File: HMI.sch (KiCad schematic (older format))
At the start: 0 parts

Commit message: Added Polyfuses and replace diodes
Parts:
- added C? (x4): 1nF, Capacitor_SMD:C_0603_1608Metric, symbol Device:C
- added F? (x2): SR010, Fuse:Fuse_0805_2012Metric, symbol Device:Polyfuse
- added F?: SR050, Fuse:Fuse_0805_2012Metric, symbol Device:Polyfuse
- added J?: Display, Connector_JST:JST_PH_B10B-PH-K_1x10_P2.00mm_Vertical, symbol Connector:Conn_01x10_Male
- added J?: SPI Interface, Connector_JST:JST_PH_B5B-PH-K_1x05_P2.00mm_Vertical, symbol Connector:Conn_01x05_Male
- added J?: I2C Interface, Connector_JST:JST_PH_B5B-PH-K_1x04_P2.00mm_Vertical, symbol Connector:Conn_01x04_Male
- added J?: Key 2, Connector_JST:JST_PH_B2B-PH-K_1x02_P2.00mm_Vertical, symbol Connector:Conn_01x02_Male
- added J?: Key 3, Connector_JST:JST_PH_B2B-PH-K_1x02_P2.00mm_Vertical, symbol Connector:Conn_01x02_Male
- added J?: Key 4, Connector_JST:JST_PH_B2B-PH-K_1x02_P2.00mm_Vertical, symbol Connector:Conn_01x02_Male
- added J?: Key 1, Connector_JST:JST_PH_B2B-PH-K_1x02_P2.00mm_Vertical, symbol Connector:Conn_01x02_Male
- added J?: LED3, Connector_JST:JST_PH_B2B-PH-K_1x02_P2.00mm_Vertical, symbol Connector:Conn_01x02_Male
- added J?: LED4, Connector_JST:JST_PH_B2B-PH-K_1x02_P2.00mm_Vertical, symbol Connector:Conn_01x02_Male
- added Q? (x2): BC817, Package_TO_SOT_SMD:SOT-23, symbol Transistor_BJT:BC817
- added R? (x2): 2.2kΩ, symbol Device:R
- added R? (x4): 4.7kΩ, Resistor_SMD:R_0603_1608Metric, symbol Device:R
- added R? (x4): 1kΩ, Resistor_SMD:R_0603_1608Metric, symbol Device:R
- added R? (x2): 4.7kΩ, symbol Device:R
- added R? (x2): 330Ω, symbol Device:R
- added RN? (x2): 330Ω, symbol Device:R_Pack04
- added U?: 74HC245, symbol 74xx:74HC245
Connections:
- new net: F?.2, J?.1 (Pin_1) (x3)
- new net: J?.2 (Pin_2), RN?.4 (R4.1)
- new net: J?.3 (Pin_3), RN?.3 (R3.1)
- new net: J?.4 (Pin_4), RN?.2 (R2.1)
- new net: J?.5 (Pin_5), RN?.1 (R1.1)
- new net: J?.6 (Pin_6), RN?.4 (R4.1)
- new net: J?.7 (Pin_7), RN?.3 (R3.1)
- new net: J?.8 (Pin_8), RN?.2 (R2.1)
- new net: RN?.8 (R1.2), U?.11 (B7)
- new net: RN?.7 (R2.2), U?.12 (B6)
- new net: RN?.6 (R3.2), U?.13 (B5)
- new net: RN?.5 (R4.2), U?.14 (B4)
- new net: RN?.8 (R1.2), U?.15 (B3)
- new net: RN?.7 (R2.2), U?.16 (B2)
- new net: RN?.6 (R3.2), U?.17 (B1)
- new net: RN?.5 (R4.2), U?.18 (B0)
- new net: J?.1 (Pin_1), R?.1, R?.2 (x4)
- new net: Q?.1 (B), R?.1 (x2)
- new net: J?.1 (Pin_1), R?.1 (x2)
- new net: J?.2 (Pin_2), Q?.3 (C) (x2)
- new net +3V3: F?.1, R?.1, R?.1
- new net +5V: F?.1, F?.1, R?.2, R?.2, R?.2, R?.2, R?.2, R?.2, U?.1 (A->B), U?.20 (VCC)
- new net GND: C?.2, C?.2, C?.2, C?.2, J?.10 (Pin_10), J?.2 (Pin_2), J?.2 (Pin_2), J?.2 (Pin_2), J?.2 (Pin_2), J?.3 (Pin_3), J?.5 (Pin_5), J?.9 (Pin_9), Q?.2 (E), Q?.2 (E), U?.10 (GND), U?.19 (CE)
- new net I2C_SCL: J?.4 (Pin_4), R?.2
- new net I2C_SDA: J?.2 (Pin_2), R?.2
- new net KEY_1: C?.1, R?.1
- new net KEY_2: C?.1, R?.1
- new net KEY_3: C?.1, R?.1
- new net KEY_4: C?.1, R?.1
- new net LCD_CON: U?.8 (A6)
- new net LCD_DB4: U?.4 (A2)
- new net LCD_DB5: U?.5 (A3)
- new net LCD_DB6: U?.6 (A4)
- new net LCD_DB7: U?.7 (A5)
- new net LCD_E: U?.3 (A1)
- new net LCD_RS: U?.2 (A0)
- new net LED3: R?.2
- new net LED4: R?.2
- new net MISO: J?.4 (Pin_4), U?.9 (A7)
- new net SPI_MISO: RN?.1 (R1.1)
- new net SPI_MOSI_BUF: J?.2 (Pin_2)
- new net SPI_SCLK_BUF: J?.3 (Pin_3)
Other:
- note added: "Buffered outputs signals"
- note added: "Check if switching is fast enought"
- note added: "Optional Keys input"
- note added: "RC Debounce"
- note added: "Wyświetlacz HD44780"
- note added: "Złącza JST PH"

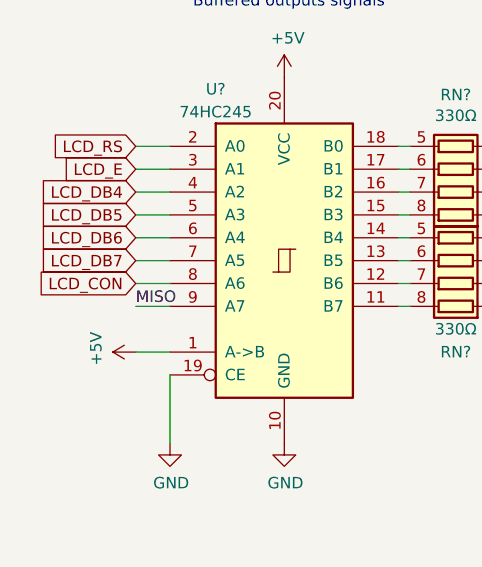
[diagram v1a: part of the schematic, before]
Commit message: Added USB B socket with ESD filter
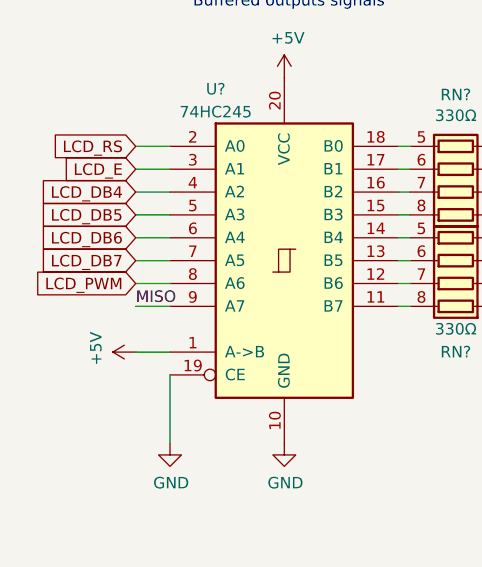
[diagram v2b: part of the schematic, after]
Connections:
- net LCD_CON renamed LCD_PWM
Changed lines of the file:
@@
 LCD_RS
 Text GLabel 1450 2250 0    50   Input ~ 0
-LCD_CON
+LCD_PWM
 Wire Wire Line
 	1450 1650 1600 1650

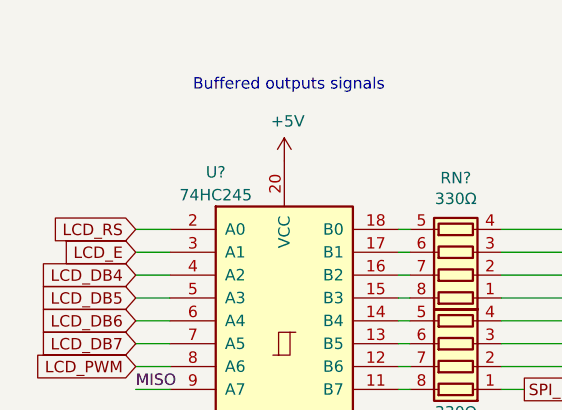
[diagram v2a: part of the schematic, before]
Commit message: Added SWD and Debug out
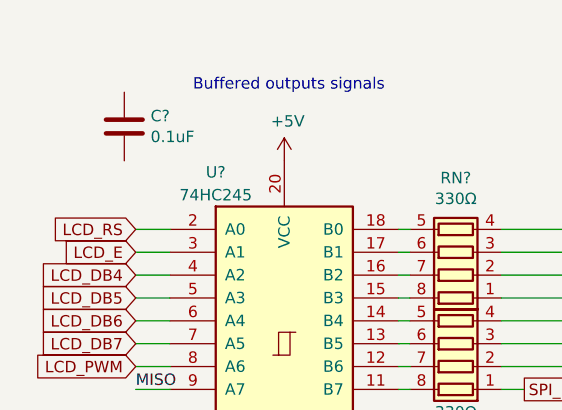
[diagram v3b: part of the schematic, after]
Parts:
- added C?: 0.1uF, Capacitor_SMD:C_0603_1608Metric, symbol Device:C
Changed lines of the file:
@@
+	1    0    0    -1
+$EndComp
+$Comp
+L Device:C C?
+U 1 1 5E465412
+P 1400 1200
+AR Path="/5E07245F/5E465412" Ref="C?"  Part="1"
+AR Path="/5E858220/5E465412" Ref="C?"  Part="1"
+AR Path="/5E91D96F/5E465412" Ref="C?"  Part="1"
+F 0 "C?" H 1515 1246 50  0000 L CNN
+F 1 "0.1uF" H 1515 1155 50  0000 L CNN
+F 2 "Capacitor_SMD:C_0603_1608Metric" H 1438 1050 50  0001 C CNN
+F 3 "~" H 1400 1200 50  0001 C CNN
+	1    1400 1200
 	1    0    0    -1
 $EndComp

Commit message: Improve schematics add new elements
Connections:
- net +5V: now also C?.1
- net GND: now also C?.2
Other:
- moved on the sheet: C?
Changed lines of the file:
@@
 L power:+5V #PWR?
 U 1 1 5E132BFD
-P 2100 1350
+P 2100 850
 AR Path="/5E07245F/5E132BFD" Ref="#PWR?"  Part="1"
 AR Path="/5E858220/5E132BFD" Ref="#PWR?"  Part="1"
 AR Path="/5E91D96F/5E132BFD" Ref="#PWR?"  Part="1"
-F 0 "#PWR?" H 2100 1200 50  0001 C CNN
-F 1 "+5V" H 2115 1523 50  0000 C CNN
-F 2 "" H 2100 1350 50  0001 C CNN
-F 3 "" H 2100 1350 50  0001 C CNN
-	1    2100 1350
+F 0 "#PWR?" H 2100 700 50  0001 C CNN
+F 1 "+5V" H 2115 1023 50  0000 C CNN
+F 2 "" H 2100 850 50  0001 C CNN
+F 3 "" H 2100 850 50  0001 C CNN
+	1    2100 850
 	1    0    0    -1
 $EndComp
@@
 Wire Wire Line
 	2600 2350 2650 2350
-Text Notes 1700 1050 0    50   ~ 0
+Text Notes 1050 1200 0    50   ~ 0
 Buffered outputs signals
 Text GLabel 1450 1850 0    50   Input ~ 0
@@
 L Device:C C?
 U 1 1 5E465412
-P 1400 1200
+P 2250 1100
 AR Path="/5E07245F/5E465412" Ref="C?"  Part="1"
 AR Path="/5E858220/5E465412" Ref="C?"  Part="1"
 AR Path="/5E91D96F/5E465412" Ref="C?"  Part="1"
-F 0 "C?" H 1515 1246 50  0000 L CNN
-F 1 "0.1uF" H 1515 1155 50  0000 L CNN
-F 2 "Capacitor_SMD:C_0603_1608Metric" H 1438 1050 50  0001 C CNN
-F 3 "~" H 1400 1200 50  0001 C CNN
-	1    1400 1200
-	1    0    0    -1
-$EndComp
+F 0 "C?" H 2365 1146 50  0000 L CNN
+F 1 "0.1uF" H 2365 1055 50  0000 L CNN
+F 2 "Capacitor_SMD:C_0603_1608Metric" H 2288 950 50  0001 C CNN
+F 3 "~" H 2250 1100 50  0001 C CNN
+	1    2250 1100
+	1    0    0    -1
+$EndComp
+Wire Wire Line
+	2100 850  2100 950
+$Comp
+L power:GND #PWR?
+U 1 1 5E2413FE
+P 2250 1250
+AR Path="/5E07245F/5E2413FE" Ref="#PWR?"  Part="1"
+AR Path="/5E858220/5E2413FE" Ref="#PWR?"  Part="1"
+AR Path="/5E91D96F/5E2413FE" Ref="#PWR?"  Part="1"
+F 0 "#PWR?" H 2250 1000 50  0001 C CNN
+F 1 "GND" H 2255 1077 50  0000 C CNN
+F 2 "" H 2250 1250 50  0001 C CNN
+F 3 "" H 2250 1250 50  0001 C CNN
+	1    2250 1250
+	1    0    0    -1
+$EndComp
+Wire Wire Line
+	2250 950  2100 950
+Connection ~ 2100 950
+Wire Wire Line
+	2100 950  2100 1350
 $EndSCHEMATC

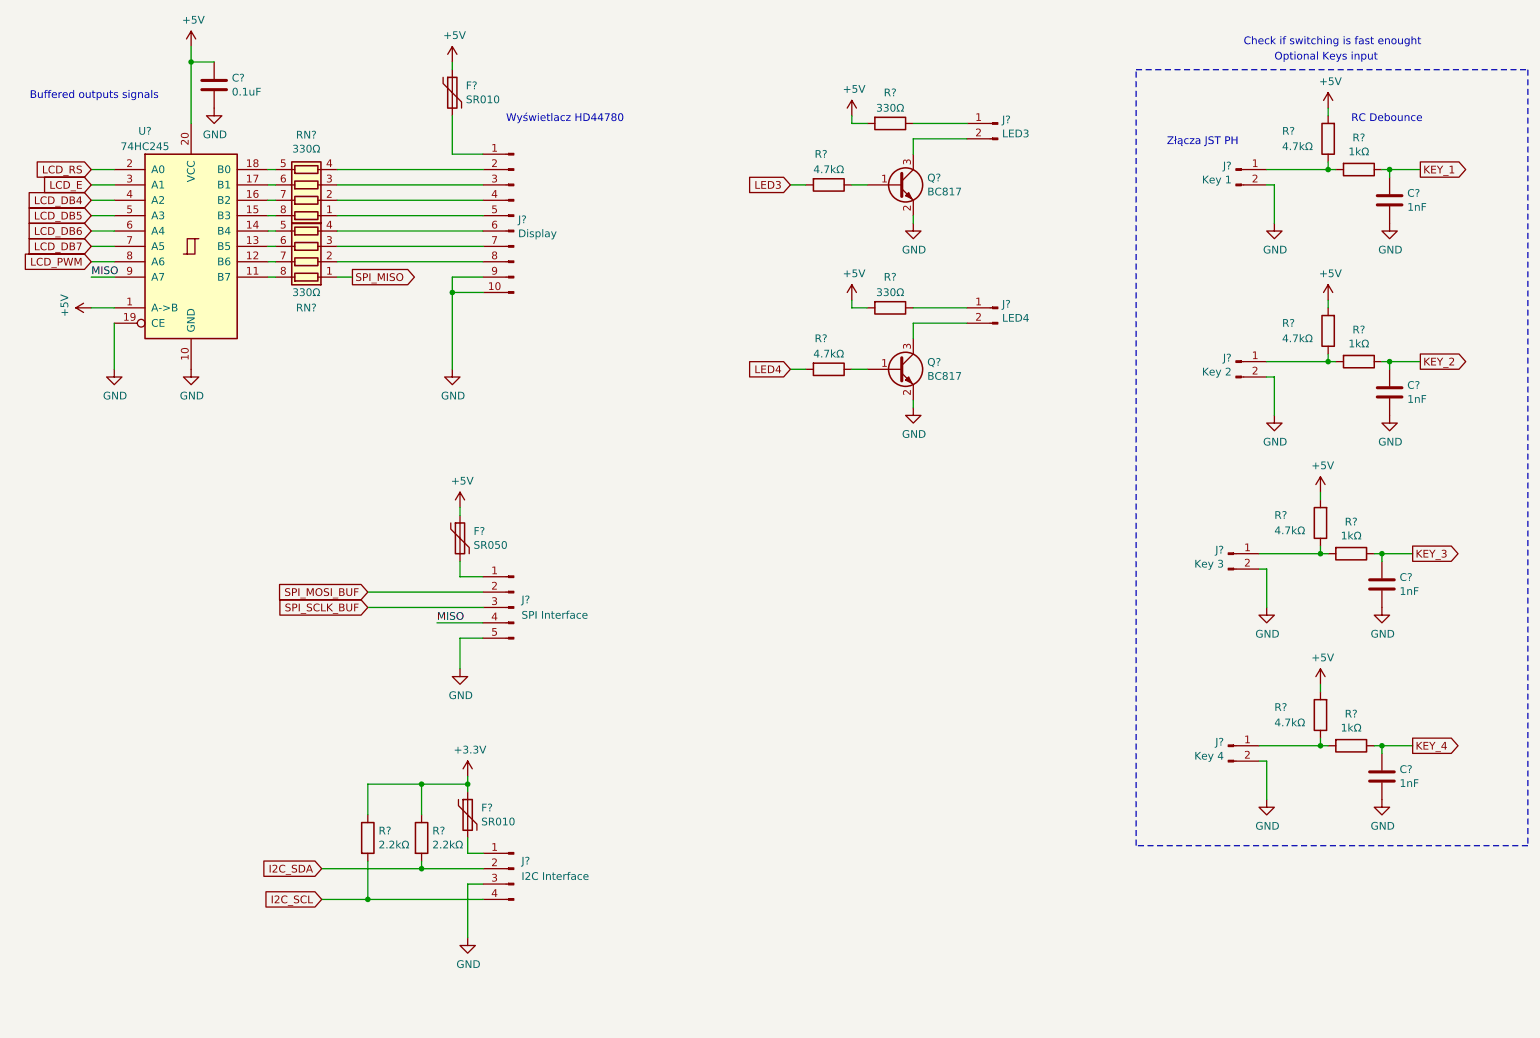
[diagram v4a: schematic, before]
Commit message: Numbering and finishing the schematic
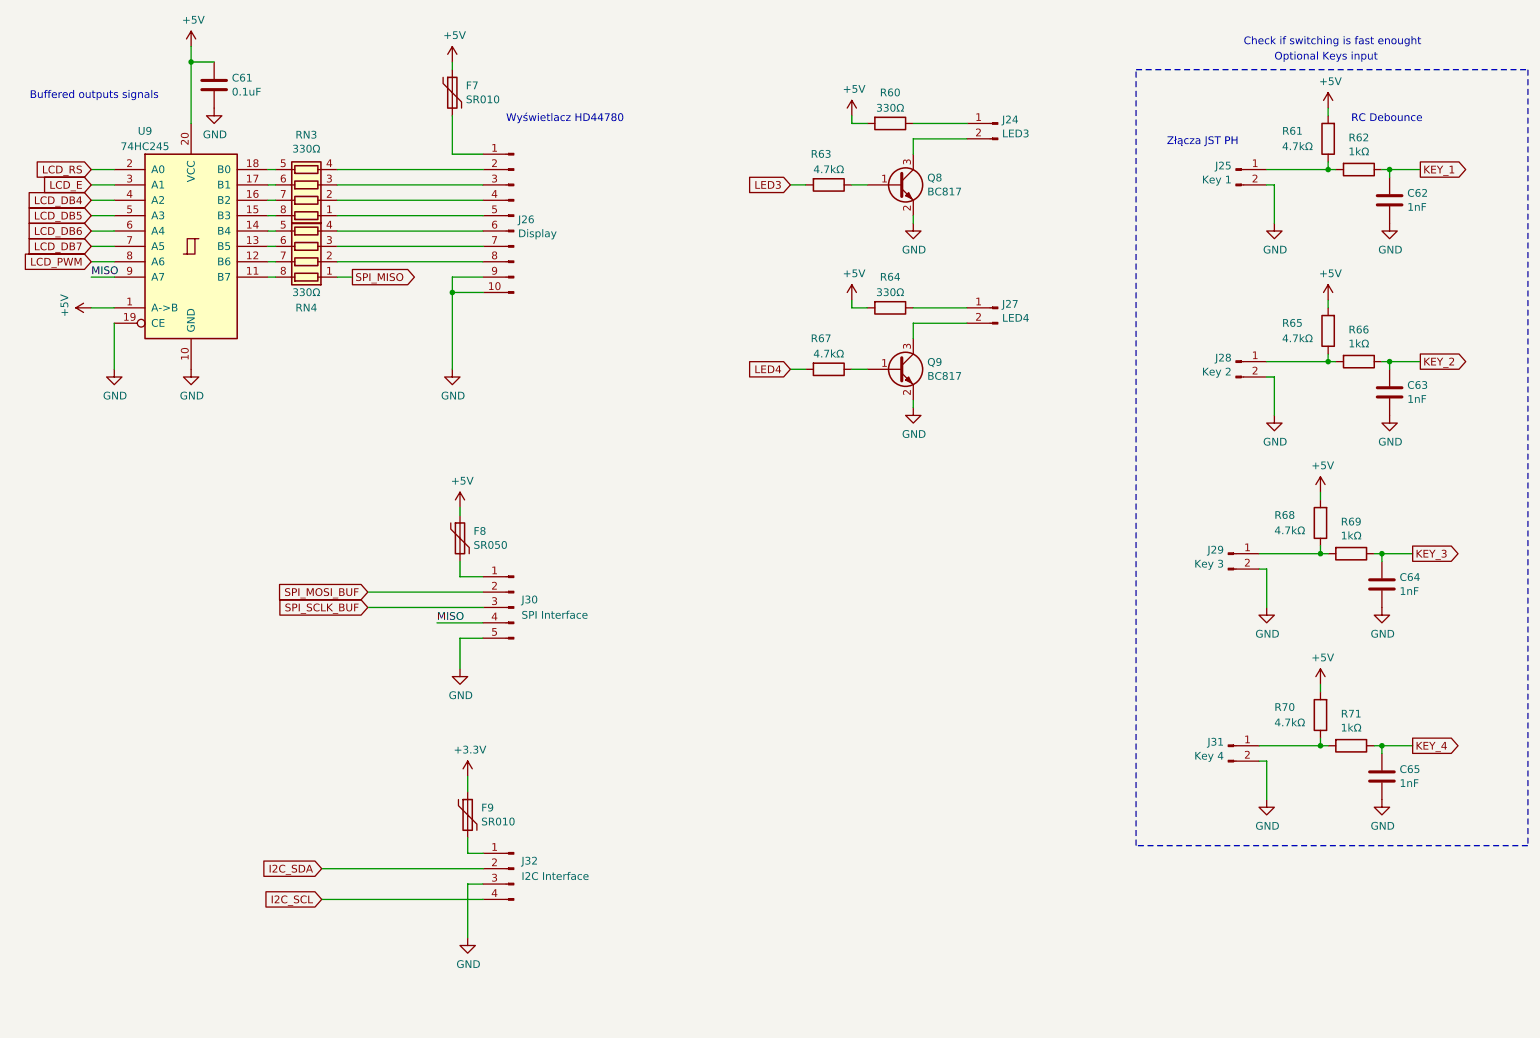
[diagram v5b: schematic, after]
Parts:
- removed R? (x2): 2.2kΩ, symbol Device:R
- gave numbers to parts that had none: 34

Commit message: Shematic almost finished, BOM in KiCad 3/4 finished
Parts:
- C63: renamed from C61; Cena (none) -> 0.05982; Dielektryk (none) -> X7R; Model (none) -> CL10B104KB8NNNC; Napięcie (none) -> 50V; Producent (none) -> SAMSUNG; Tolerancja (none) -> 10%; Typ (none) -> SMD
- F7, F9: Cena (none) -> 0.6152; Link (none) -> https://www.tme.eu/pl/details/sr010-15/bezpieczniki-polimer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; Model (none) -> SR010-15; Opis (none) -> Bezpiecznik: polimerowy PTC; 100mA; Obud: 0805; Producent (none) -> ECE; Typ (none) -> SMD
- F8: Cena (none) -> 0.9060; Link (none) -> https://www.tme.eu/pl/details/sr050-06/bezpieczniki-polimer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; Model (none) -> SR050-06; Opis (none) -> Bezpiecznik: polimerowy PTC; 500mA; Obud: 0805; Producent (none) -> ECE; Typ (none) -> SMD
- J26: renamed from J32; footprint Connector_JST:JST_PH_B5B-PH-K_1x04_P2.00mm_Vertical -> Connector_JST:JST_PH_B4B-PH-K_1x04_P2.00mm_Vertical
- J27: renamed from J24; Cena (none) -> 0.47429; Link (none) -> https://www.tme.eu/pl/details/b2b-ph-k-s/zlacza-sygnalowe-r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; Model (none) -> B2B-PH-K-S; Opis (none) -> Gniazdo; przewód-płytka; męskie; PH; 2mm; PIN: 2; THT; 100V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; Producent (none) -> JST; Typ (none) -> THT
- J28: renamed from J27; Cena (none) -> 0.47429; Link (none) -> https://www.tme.eu/pl/details/b2b-ph-k-s/zlacza-sygnalowe-r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; Model (none) -> B2B-PH-K-S; Opis (none) -> Gniazdo; przewód-płytka; męskie; PH; 2mm; PIN: 2; THT; 100V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; Producent (none) -> JST; Typ (none) -> THT
- J29: Cena (none) -> 0.47429; Link (none) -> https://www.tme.eu/pl/details/b2b-ph-k-s/zlacza-sygnalowe-r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; Model (none) -> B2B-PH-K-S; Opis (none) -> Gniazdo; przewód-płytka; męskie; PH; 2mm; PIN: 2; THT; 100V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; Producent (none) -> JST; Typ (none) -> THT
- J30: renamed from J31; Cena (none) -> 0.47429; Link (none) -> https://www.tme.eu/pl/details/b2b-ph-k-s/zlacza-sygnalowe-r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; Model (none) -> B2B-PH-K-S; Opis (none) -> Gniazdo; przewód-płytka; męskie; PH; 2mm; PIN: 2; THT; 100V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; Producent (none) -> JST; Typ (none) -> THT
- J31: renamed from J25; Cena (none) -> 0.47429; Link (none) -> https://www.tme.eu/pl/details/b2b-ph-k-s/zlacza-sygnalowe-r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; Model (none) -> B2B-PH-K-S; Opis (none) -> Gniazdo; przewód-płytka; męskie; PH; 2mm; PIN: 2; THT; 100V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; Producent (none) -> JST; Typ (none) -> THT
- J32: renamed from J28; Cena (none) -> 0.47429; Link (none) -> https://www.tme.eu/pl/details/b2b-ph-k-s/zlacza-sygnalowe-r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; Model (none) -> B2B-PH-K-S; Opis (none) -> Gniazdo; przewód-płytka; męskie; PH; 2mm; PIN: 2; THT; 100V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; Producent (none) -> JST; Typ (none) -> THT
- R60: renamed from R63; footprint (none) -> Resistor_SMD:R_0603_1608Metric
- R61: renamed from R67; footprint (none) -> Resistor_SMD:R_0603_1608Metric
- R62: renamed from R60; footprint (none) -> Resistor_SMD:R_0603_1608Metric
- R63: renamed from R64; footprint (none) -> Resistor_SMD:R_0603_1608Metric
- RN3, RN4: footprint (none) -> Resistor_SMD:R_Array_Convex_4x0603; Cena (none) -> 0.04823; Link (none) -> https://www.tme.eu/pl/details/dr1206-330r-4_8/drabinki-rezy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; Model (none) -> 4D03WGJ0331T; Opis (none) -> Drabinka rezystorowa: Y; 330Ω; SMD; 1206; Il.rezystorów: 4;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; Producent (none) -> ROYAL OHM; Typ (none) -> SMD
- U9: footprint (none) -> Package_SO:TSSOP-20_4.4x6.5mm_P0.65mm; Cena (none) -> 0.9740; Link (none) -> https://www.tme.eu/pl/details/74hc245pw.112/bufory-nadajnik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; Model (none) -> 74HC245PW.112; Opis (none) -> IC: cyfrowy; bus transceiver; Kanały: 8; SMD; TSSOP20; Seri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; Producent (none) -> NEXPERIA; Typ (none) -> SMD
- renumbered C62 to C66, C63 to C67, J26 to J24, J30 to J25, R68 to R64, R70 to R65, R61 to R66, R65 to R67, R69 to R68, R71 to R69, R62 to R70, R66 to R71

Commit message: BOM in KiCad almost finished, genereated NETLIST, create PCB
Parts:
- C64, C65, C66, C67: Cena (none) -> 0.05563; Link (none) -> https://www.tme.eu/pl/details/cl10b102kb8nnnc/kondensatory-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; Model (none) -> CL10B102KB8NNNC; Opis (none) -> Kondensator: ceramiczny; MLCC; 1nF; 50V; X7R; ±10%; SMD; 06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; Producent (none) -> SAMSUNG; Typ (none) -> SMD
- J24: Cena (none) -> 1.33; Link (none) -> https://pl.farnell.com/jst-japan-solderless-terminals/b10b-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; Model (none) -> B10B-PH-K-S; Opis (none) -> Złącze przewód-płytka, pionowe, 2 mm, 10 styki/-ów, Header,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; Producent (none) -> JST; Typ (none) -> THT
- J25: Cena (none) -> 0.90501; Link (none) -> https://www.tme.eu/pl/details/b5b-ph-k-s/zlacza-sygnalowe-r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; Model (none) -> B5B-PH-K-S; Opis (none) -> Gniazdo; przewód-płytka; męskie; PH; 2mm; PIN: 5; THT; 100V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; Producent (none) -> JST; Typ (none) -> THT
- J26: Cena (none) -> 0.78136; Link (none) -> https://www.tme.eu/pl/details/b4b-ph-k-s/zlacza-sygnalowe-r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; Model (none) -> B4B-PH-K-S; Opis (none) -> Gniazdo; przewód-płytka; męskie; PH; 2mm; PIN: 4; THT; 100V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; Producent (none) -> JST; Typ (none) -> THT
- Q8, Q9: Cena (none) -> 0.1189; Link (none) -> https://www.tme.eu/pl/details/bc817.215/tranzystory-npn-smd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; Model (none) -> BC817.215; Opis (none) -> Tranzystor: NPN; bipolarny; 45V; 0,5A; 250mW; SOT23; Producent (none) -> NEXPERIA; Typ (none) -> SMD
- R60, R61, R64, R65, R66, R67: Cena (none) -> 0.04651; Link (none) -> https://www.tme.eu/pl/details/smd0603-4k7-1%25/rezystory-sm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; Model (none) -> SMD0603-4K7-1%; Opis (none) -> Rezystor: thick film; SMD; 0603; 4,7kΩ; 0,1W; ±1%; -55÷155°C; Producent (none) -> ROYAL OHM; Typ (none) -> SMD
- R62, R63: Cena (none) -> 0.04651; Typ (none) -> SMD
- R68, R69, R70, R71: Cena (none) -> 0.04651; Link (none) -> https://www.tme.eu/pl/details/smd0603-1k-1%25/rezystory-smd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; Model (none) -> 0603SAF1001T5E; Opis (none) -> Rezystor: thick film; SMD; 0603; 1kΩ; 0,1W; ±1%; -55÷155°C; Producent (none) -> ROYAL OHM; Typ (none) -> SMD
